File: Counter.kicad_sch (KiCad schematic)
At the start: 14 parts, among them SW2 SW_Push, SW3 SW_Push, SW4 SW_Push, U10 74LS160, U11 74LS160, U12 74LS160, U13 74LS160, U14 74LS160, U5 74LS10, U8 74LS20, U9 74LS160

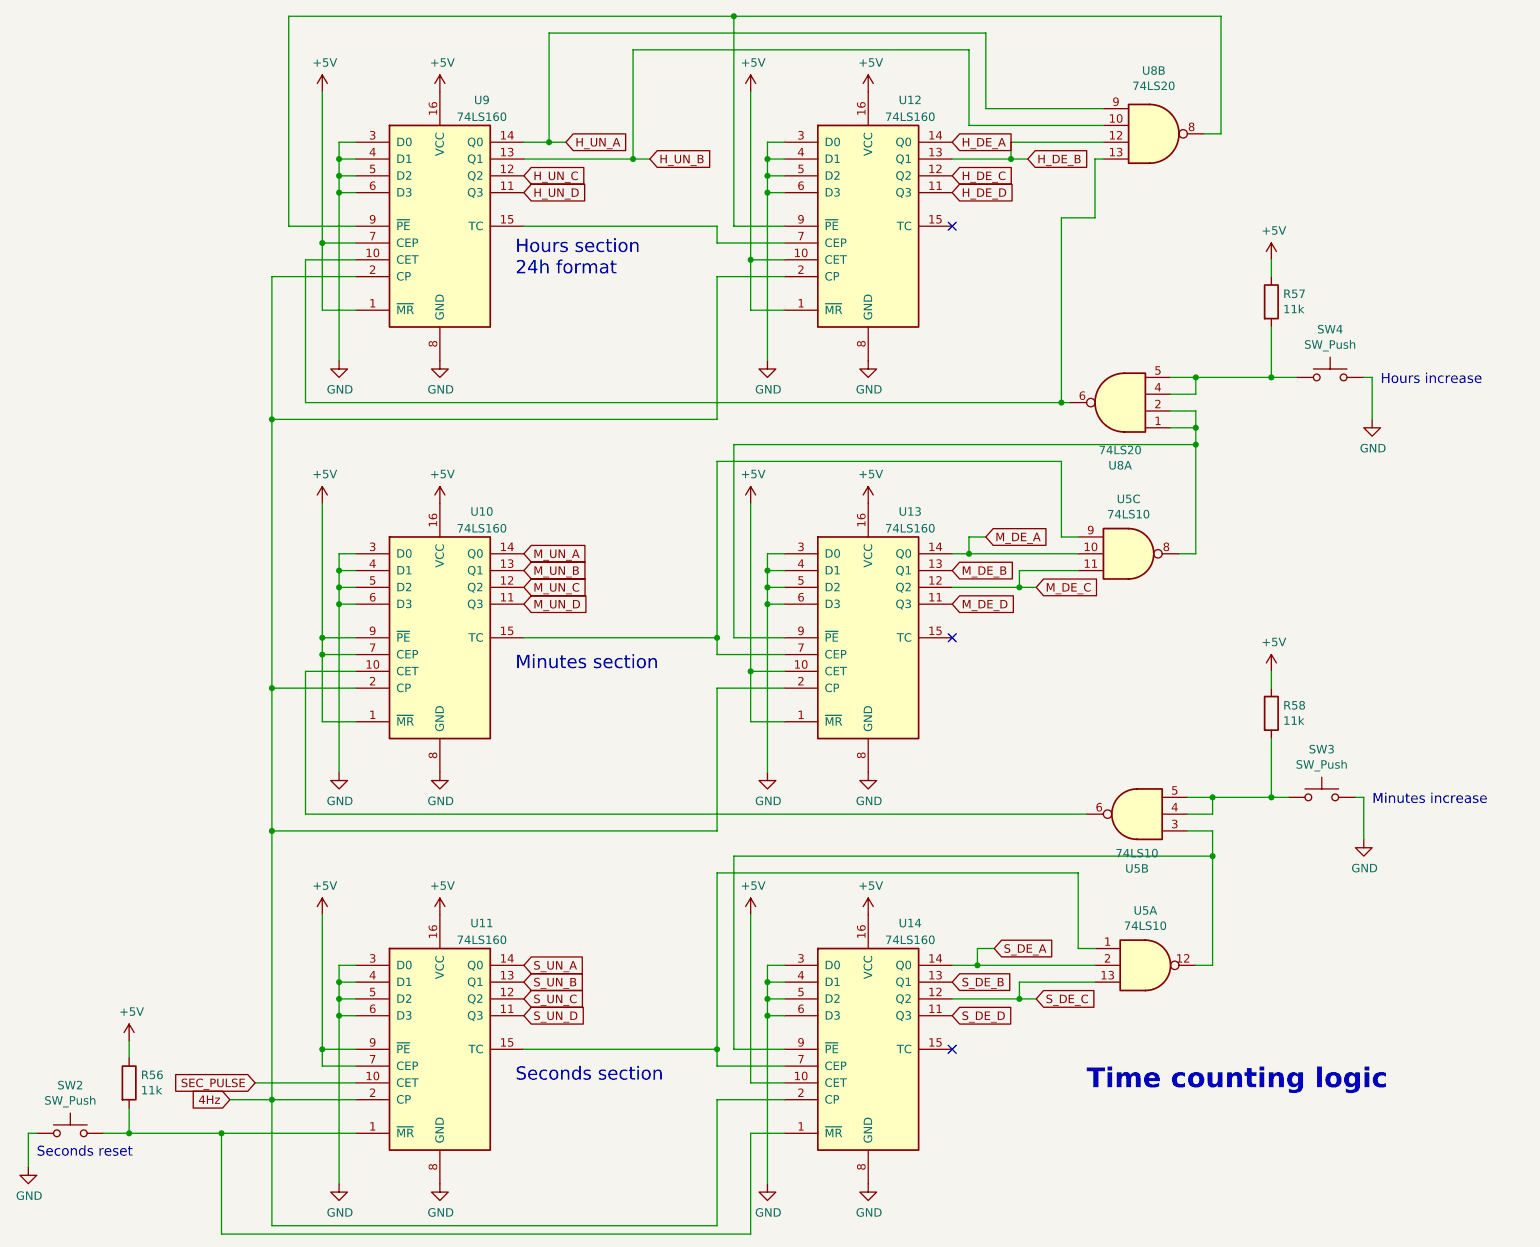
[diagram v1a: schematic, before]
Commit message: Pablo's review, several changes:
Schematic:
- Overall aesthetics
- Added PWR_FLAG to remove ERC errors.
Layout:
- Overall component alignment
- Removed some loops and unnecessary vias.
- Cleaned up vias without ends.
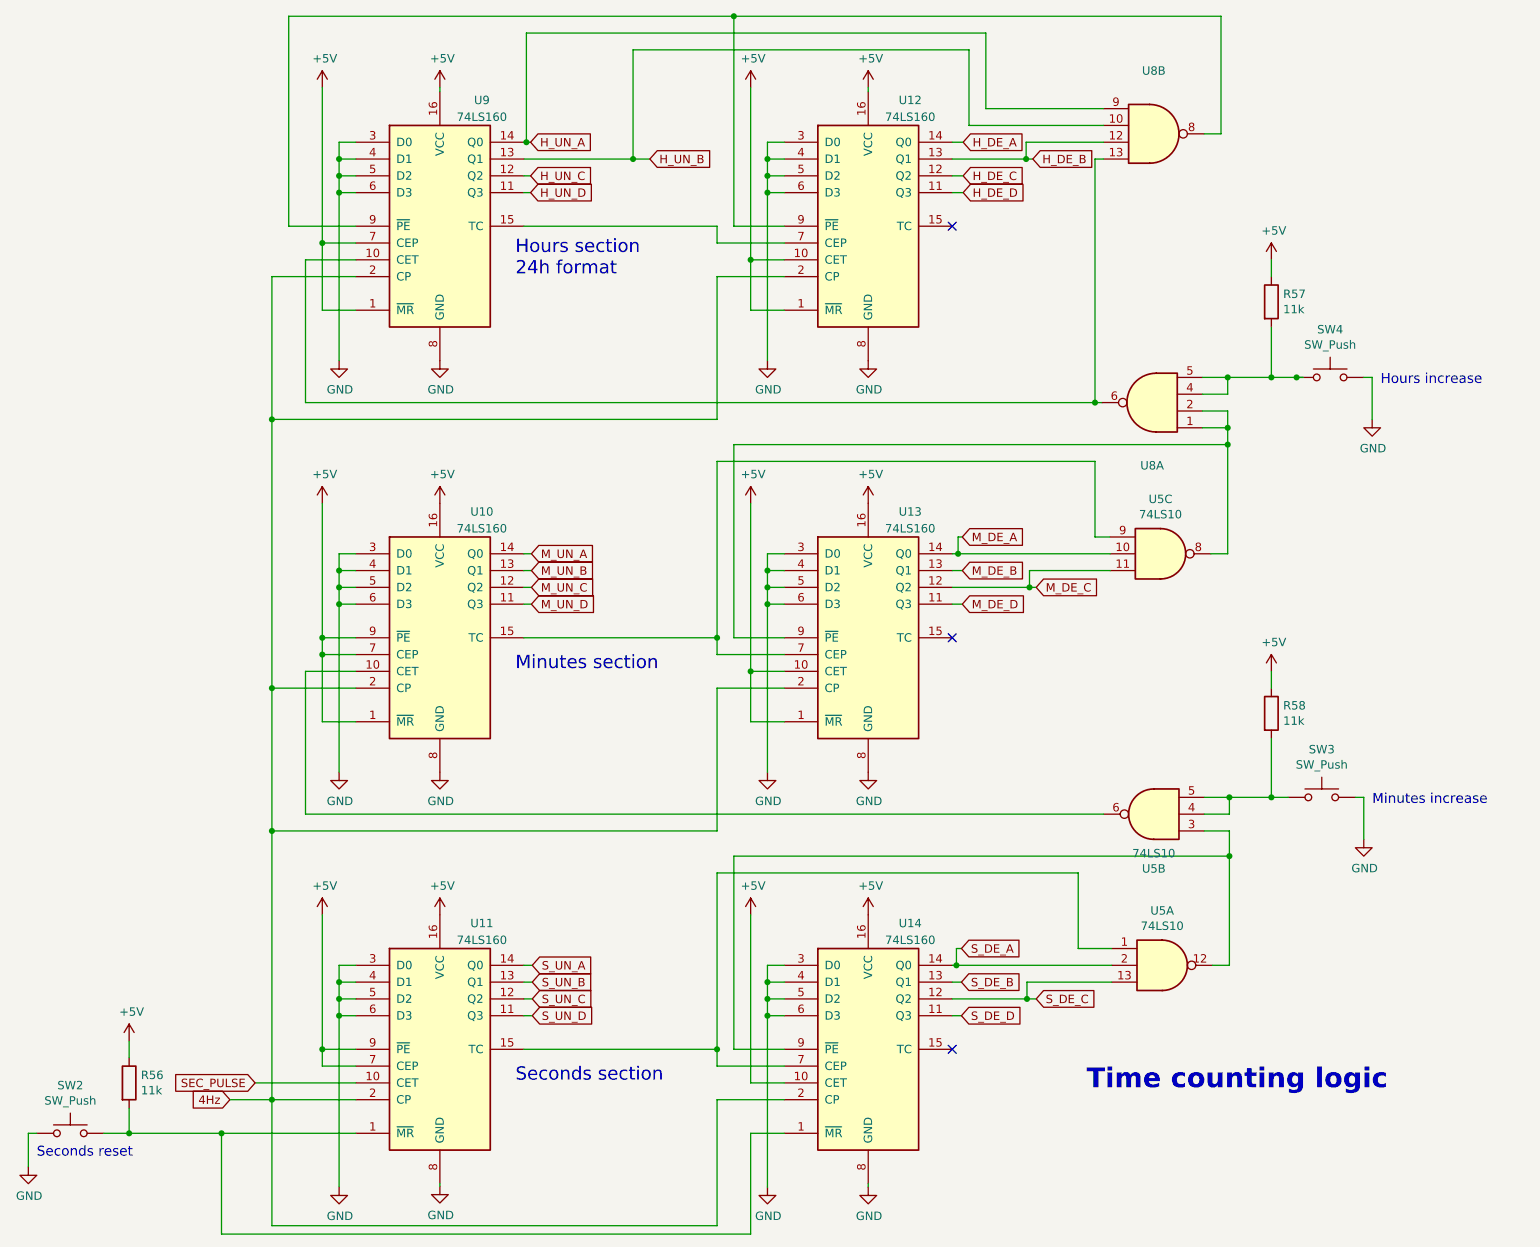
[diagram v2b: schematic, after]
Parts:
- U8: value 74LS20 -> (none); footprint Package_DIP:DIP-14_W7.62mm -> (none)
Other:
- moved on the sheet: U5A, U5B, U5C, U8A

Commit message: WIP
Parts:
- removed R56: 11k, Resistor_THT:R_Axial_DIN0207_L6.3mm_D2.5mm_P10.16mm_Horizontal, symbol Device:R
- removed SW2: SW_Push, Button_Switch_THT:SW_Tactile_SPST_Angled_PTS645Vx83-2LFS, symbol Switch:SW_Push
- R57, R58: footprint Resistor_THT:R_Axial_DIN0207_L6.3mm_D2.5mm_P10.16mm_Horizontal -> Resistor_SMD:R_0805_2012Metric
- U8: value (none) -> 74LS20; footprint (none) -> Package_DIP:DIP-14_W7.62mm
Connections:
- net +5V: now also U11.1 (~{MR}), U14.1 (~{MR})
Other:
- note removed: "Seconds reset"
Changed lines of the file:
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@@
     (rev "0")
   )
-  (junction (at 49.53 181.61) (diameter 0) (color 0 0 0 0)
-  )
   (junction (at 127 12.7) (diameter 0) (color 0 0 0 0)
   )
@@
   (junction (at 132.08 96.52) (diameter 0) (color 0 0 0 0)
   )
-  (junction (at 35.56 181.61) (diameter 0) (color 0 0 0 0)
-  )
   (junction (at 64.77 106.68) (diameter 0) (color 0 0 0 0)
   )
-  (junction (at 212.09 67.31) (diameter 0) (color 0 0 0 0)
+  (junction (at 129.54 173.99) (diameter 0) (color 0 0 0 0)
   )
   (junction (at 64.77 109.22) (diameter 0) (color 0 0 0 0)
@@
   )
   (junction (at 208.28 130.81) (diameter 0) (color 0 0 0 0)
+  )
+  (junction (at 64.77 171.45) (diameter 0) (color 0 0 0 0)
   )
   (junction (at 67.31 96.52) (diameter 0) (color 0 0 0 0)
@@
     (stroke (width 0) (type default) (color 0 0 0 0))
   )
+  (wire (pts (xy 64.77 171.45) (xy 64.77 181.61))
+    (stroke (width 0) (type default) (color 0 0 0 0))
+  )
   (wire (pts (xy 134.62 119.38) (xy 129.54 119.38))
     (stroke (width 0) (type default) (color 0 0 0 0))
@@
     (stroke (width 0) (type default) (color 0 0 0 0))
   )
-  (wire (pts (xy 49.53 181.61) (xy 69.85 181.61))
-    (stroke (width 0) (type default) (color 0 0 0 0))
-  )
   (wire (pts (xy 96.393 101.6) (xy 95.25 101.6))
     (stroke (width 0) (type default) (color 0 0 0 0))
@@
     (stroke (width 0) (type default) (color 0 0 0 0))
   )
-  (wire (pts (xy 20.32 186.69) (xy 20.32 181.61))
-    (stroke (width 0) (type default) (color 0 0 0 0))
-  )
   (wire (pts (xy 124.46 142.24) (xy 179.07 142.24))
     (stroke (width 0) (type default) (color 0 0 0 0))
@@
     (stroke (width 0) (type default) (color 0 0 0 0))
   )
-  (wire (pts (xy 35.56 181.61) (xy 49.53 181.61))
-    (stroke (width 0) (type default) (color 0 0 0 0))
-  )
   (wire (pts (xy 69.85 156.21) (xy 67.31 156.21))
     (stroke (width 0) (type default) (color 0 0 0 0))
@@
     (stroke (width 0) (type default) (color 0 0 0 0))
   )
-  (wire (pts (xy 20.32 181.61) (xy 21.59 181.61))
-    (stroke (width 0) (type default) (color 0 0 0 0))
-  )
-  (wire (pts (xy 49.53 196.85) (xy 129.54 196.85))
-    (stroke (width 0) (type default) (color 0 0 0 0))
-  )
   (wire (pts (xy 200.66 12.7) (xy 127 12.7))
     (stroke (width 0) (type default) (color 0 0 0 0))
@@
     (stroke (width 0) (type default) (color 0 0 0 0))
   )
-  (wire (pts (xy 31.75 181.61) (xy 35.56 181.61))
-    (stroke (width 0) (type default) (color 0 0 0 0))
-  )
   (wire (pts (xy 208.28 130.81) (xy 210.82 130.81))
     (stroke (width 0) (type default) (color 0 0 0 0))
@@
     (stroke (width 0) (type default) (color 0 0 0 0))
   )
-  (wire (pts (xy 49.53 181.61) (xy 49.53 196.85))
-    (stroke (width 0) (type default) (color 0 0 0 0))
-  )
   (wire (pts (xy 69.85 39.37) (xy 67.31 39.37))
     (stroke (width 0) (type default) (color 0 0 0 0))
@@
     (stroke (width 0) (type default) (color 0 0 0 0))
   )
-  (wire (pts (xy 129.54 196.85) (xy 129.54 181.61))
-    (stroke (width 0) (type default) (color 0 0 0 0))
-  )
   (wire (pts (xy 129.54 57.15) (xy 134.62 57.15))
     (stroke (width 0) (type default) (color 0 0 0 0))
@@
     (stroke (width 0) (type default) (color 0 0 0 0))
   )
-  (wire (pts (xy 212.09 67.31) (xy 213.106 67.31))
-    (stroke (width 0) (type default) (color 0 0 0 0))
-  )
   (wire (pts (xy 129.54 119.38) (xy 129.54 111.76))
     (stroke (width 0) (type default) (color 0 0 0 0))
@@
     (stroke (width 0) (type default) (color 0 0 0 0))
   )
-  (wire (pts (xy 35.56 181.61) (xy 35.56 177.8))
-    (stroke (width 0) (type default) (color 0 0 0 0))
-  )
   (wire (pts (xy 201.93 135.89) (xy 198.12 135.89))
     (stroke (width 0) (type default) (color 0 0 0 0))
@@
     (stroke (width 0) (type default) (color 0 0 0 0))
   )
-  (wire (pts (xy 35.56 167.64) (xy 35.56 170.18))
+  (wire (pts (xy 129.54 173.99) (xy 129.54 181.61))
     (stroke (width 0) (type default) (color 0 0 0 0))
   )
@@
   )
   (wire (pts (xy 62.23 133.35) (xy 62.23 111.76))
+    (stroke (width 0) (type default) (color 0 0 0 0))
+  )
+  (wire (pts (xy 64.77 181.61) (xy 69.85 181.61))
     (stroke (width 0) (type default) (color 0 0 0 0))
   )
@@
   (text "Time counting logic" (at 180.34 175.26 0)
     (effects (font (size 2.9972 2.9972) (thickness 0.5994) bold) (justify left bottom))
-  )
-  (text "Seconds reset" (at 21.59 185.42 0)
-    (effects (font (size 1.4986 1.4986)) (justify left bottom))
   )
   (text "Hours increase" (at 224.79 68.58 0)
@@
       (effects (font (size 1.27 1.27)) hide)
     )
-  )
-  (symbol (lib_id "Switch:SW_Push") (at 26.67 181.61 0) (unit 1)
-    (in_bom yes) (on_board yes)
-    (property "Reference" "SW2" (id 0) (at 26.67 174.371 0))
-    (property "Value" "SW_Push" (id 1) (at 26.67 176.6824 0))
-    (property "Footprint" "Button_Switch_THT:SW_Tactile_SPST_Angled_PTS645Vx83-2LFS" (id 2) (at 26.67 176.53 0)
-      (effects (font (size 1.27 1.27)) hide)
-    )
-    (property "Datasheet" "~" (id 3) (at 26.67 176.53 0)
-      (effects (font (size 1.27 1.27)) hide)
-    )
-    (pin "1")
-    (pin "2")
   )
   (symbol (lib_id "Switch:SW_Push") (at 215.9 130.81 0) (unit 1)
@@
       (effects (font (size 1.27 1.27)) (justify left))
     )
-    (property "Footprint" "Resistor_THT:R_Axial_DIN0207_L6.3mm_D2.5mm_P10.16mm_Horizontal" (id 2) (at 206.502 55.88 90)
+    (property "Footprint" "Resistor_SMD:R_0805_2012Metric" (id 2) (at 206.502 55.88 90)
       (effects (font (size 1.27 1.27)) hide)
     )
@@
       (effects (font (size 1.27 1.27)) (justify left))
     )
-    (property "Footprint" "Resistor_THT:R_Axial_DIN0207_L6.3mm_D2.5mm_P10.16mm_Horizontal" (id 2) (at 206.502 118.11 90)
+    (property "Footprint" "Resistor_SMD:R_0805_2012Metric" (id 2) (at 206.502 118.11 90)
       (effects (font (size 1.27 1.27)) hide)
     )
     (property "Datasheet" "~" (id 3) (at 208.28 118.11 0)
-      (effects (font (size 1.27 1.27)) hide)
-    )
-    (pin "1")
-    (pin "2")
-  )
-  (symbol (lib_id "Device:R") (at 35.56 173.99 0) (unit 1)
-    (in_bom yes) (on_board yes)
-    (property "Reference" "R56" (id 0) (at 37.338 172.8216 0)
-      (effects (font (size 1.27 1.27)) (justify left))
-    )
-    (property "Value" "11k" (id 1) (at 37.338 175.133 0)
-      (effects (font (size 1.27 1.27)) (justify left))
-    )
-    (property "Footprint" "Resistor_THT:R_Axial_DIN0207_L6.3mm_D2.5mm_P10.16mm_Horizontal" (id 2) (at 33.782 173.99 90)
-      (effects (font (size 1.27 1.27)) hide)
-    )
-    (property "Datasheet" "~" (id 3) (at 35.56 173.99 0)
       (effects (font (size 1.27 1.27)) hide)
     )
@@
     (pin "1")
   )
-  (symbol (lib_id "power:+5V") (at 35.56 167.64 0) (unit 1)
-    (in_bom yes) (on_board yes)
-    (property "Reference" "#PWR094" (id 0) (at 35.56 171.45 0)
-      (effects (font (size 1.27 1.27)) hide)
-    )
-    (property "Value" "+5V" (id 1) (at 35.941 163.2458 0))
-    (property "Footprint" "" (id 2) (at 35.56 167.64 0)
-      (effects (font (size 1.27 1.27)) hide)
-    )
-    (property "Datasheet" "" (id 3) (at 35.56 167.64 0)
-      (effects (font (size 1.27 1.27)) hide)
-    )
-    (pin "1")
-  )
   (symbol (lib_id "power:GND") (at 223.52 73.66 0) (unit 1)
     (in_bom yes) (on_board yes)
@@
     (pin "1")
   )
-  (symbol (lib_id "power:GND") (at 20.32 186.69 0) (unit 1)
-    (in_bom yes) (on_board yes)
-    (property "Reference" "#PWR093" (id 0) (at 20.32 193.04 0)
-      (effects (font (size 1.27 1.27)) hide)
-    )
-    (property "Value" "GND" (id 1) (at 20.447 191.0842 0))
-    (property "Footprint" "" (id 2) (at 20.32 186.69 0)
-      (effects (font (size 1.27 1.27)) hide)
-    )
-    (property "Datasheet" "" (id 3) (at 20.32 186.69 0)
-      (effects (font (size 1.27 1.27)) hide)
-    )
-    (pin "1")
-  )
   (symbol (lib_name "74LS20_1") (lib_id "74xx:74LS20") (at 190.246 71.12 180) (unit 1)
     (in_bom yes) (on_board yes)
     (property "Reference" "U8" (id 0) (at 190.246 80.645 0))
-    (property "Value" "" (id 1) (at 190.246 78.3336 0))
-    (property "Footprint" "" (id 2) (at 190.246 71.12 0)
+    (property "Value" "74LS20" (id 1) (at 190.246 78.3336 0))
+    (property "Footprint" "Package_DIP:DIP-14_W7.62mm" (id 2) (at 190.246 71.12 0)
       (effects (font (size 1.27 1.27)) hide)
     )
@@
     (in_bom yes) (on_board yes)
     (property "Reference" "U8" (id 0) (at 190.5 20.955 0))
-    (property "Value" "" (id 1) (at 190.5 23.2664 0))
-    (property "Footprint" "" (id 2) (at 190.5 30.48 0)
-      (effects (font (size 1.27 1.27)) hide)
-    )
+    (property "Value" "74LS20" (id 1) (at 190.5 23.2664 0))
+    (property "Footprint" "Package_DIP:DIP-14_W7.62mm" (id 2) (at 190.5 30.48 0)
+      (effects (font (size 1.27 1.27)) hide)
+    )
